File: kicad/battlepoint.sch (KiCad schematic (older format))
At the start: 26 parts, among them J1 BTNS, J2 TMR_LEDS, J3 CAP_LEDS, P13 BTNS_IN, P14 OLED_OUT, P17 BTNS_OUT, P20 AUX_PWR, P30 EXT_PWR_JP, P5 SPK, P8 AUDIO_JACK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

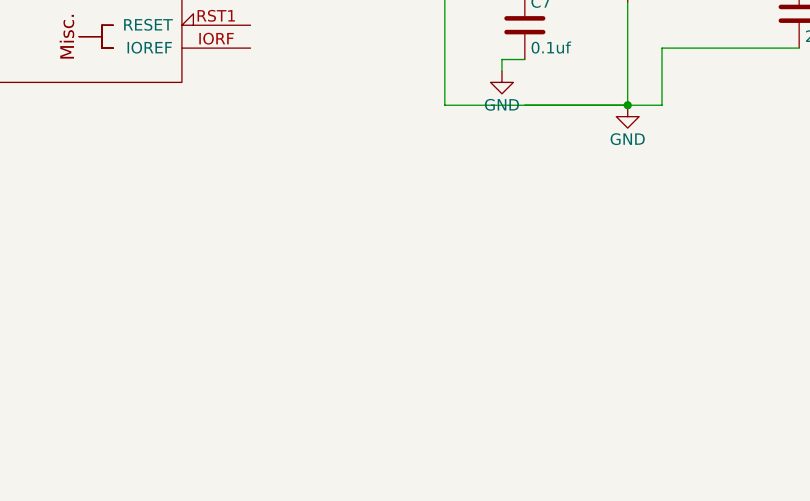
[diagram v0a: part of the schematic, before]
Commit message: reversed the top layer
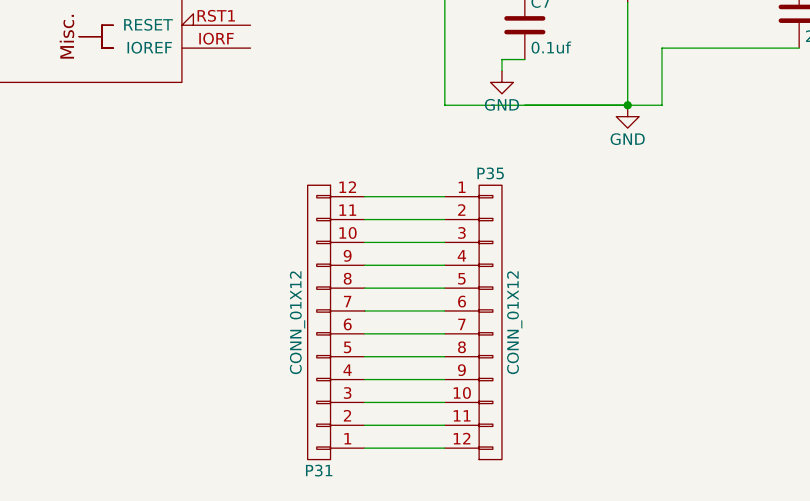
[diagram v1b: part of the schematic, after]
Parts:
- added P31, P35: CONN_01X12, Pin_Headers:Pin_Header_Straight_1x12, symbol CONN_01X12
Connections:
- new net: P31.1 (P1), P35.12 (P12)
- new net: P31.10 (P10), P35.3 (P3)
- new net: P31.11 (P11), P35.2 (P2)
- new net: P31.12 (P12), P35.1 (P1)
- new net: P31.2 (P2), P35.11 (P11)
- new net: P31.3 (P3), P35.10 (P10)
- new net: P31.4 (P4), P35.9 (P9)
- new net: P31.5 (P5), P35.8 (P8)
- new net: P31.6 (P6), P35.7 (P7)
- new net: P31.7 (P7), P35.6 (P6)
- new net: P31.8 (P8), P35.5 (P5)
- new net: P31.9 (P9), P35.4 (P4)

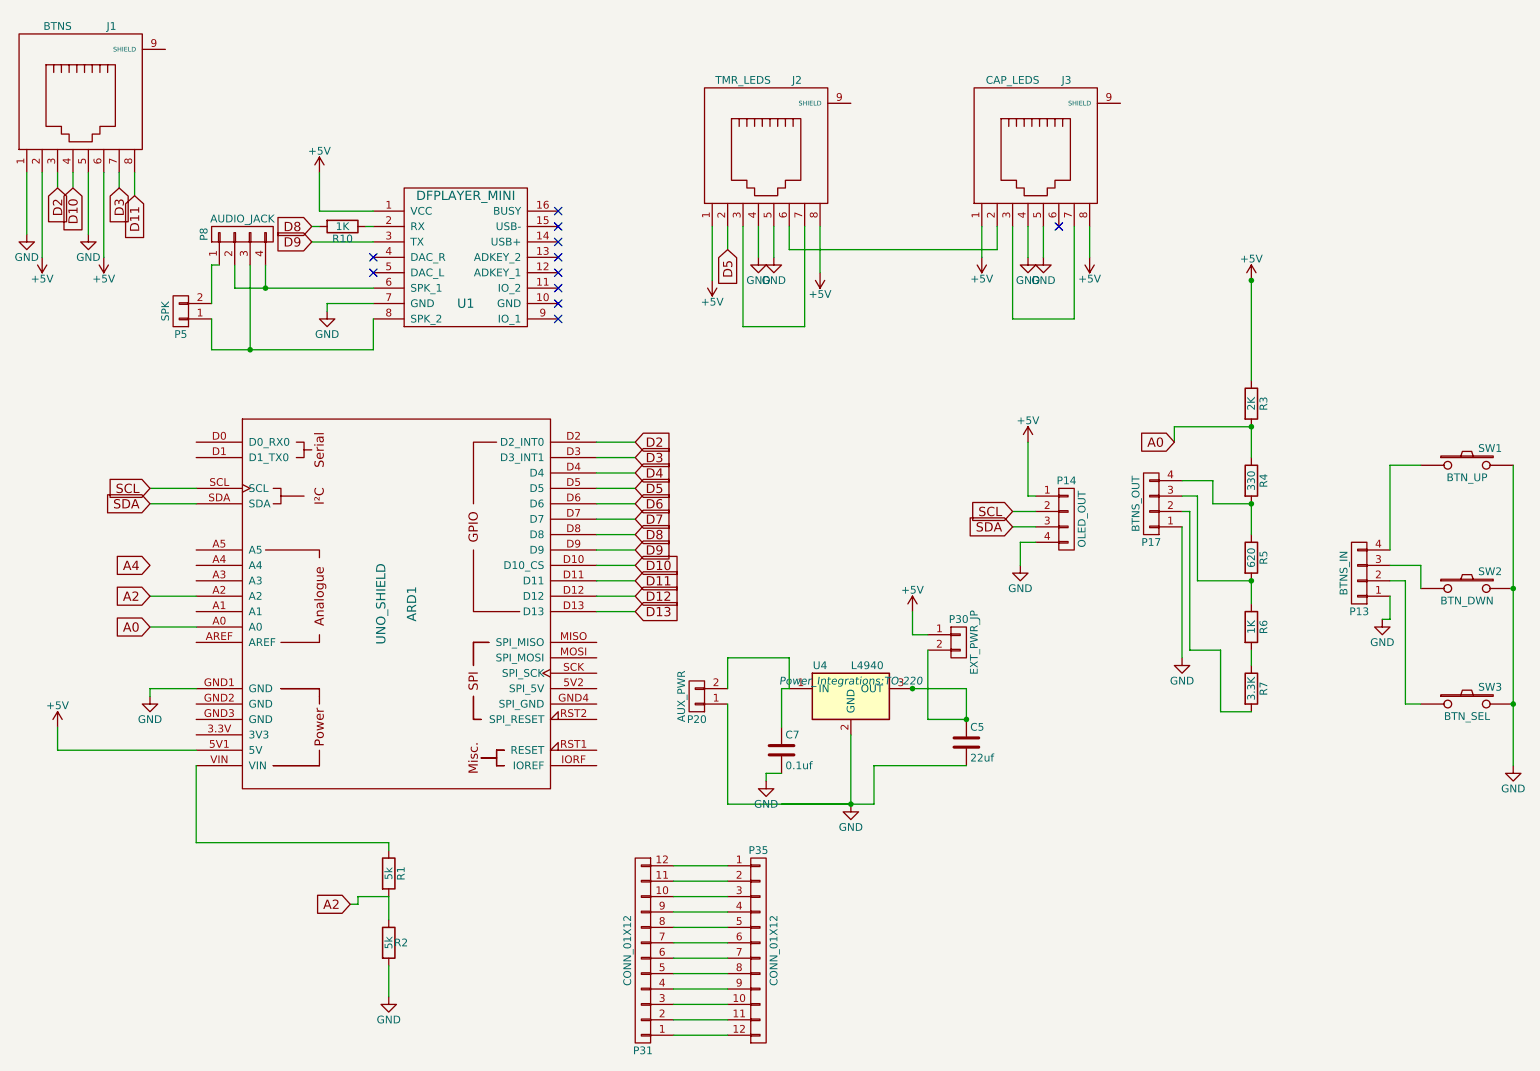
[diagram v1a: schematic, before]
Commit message: changed to usb connectors
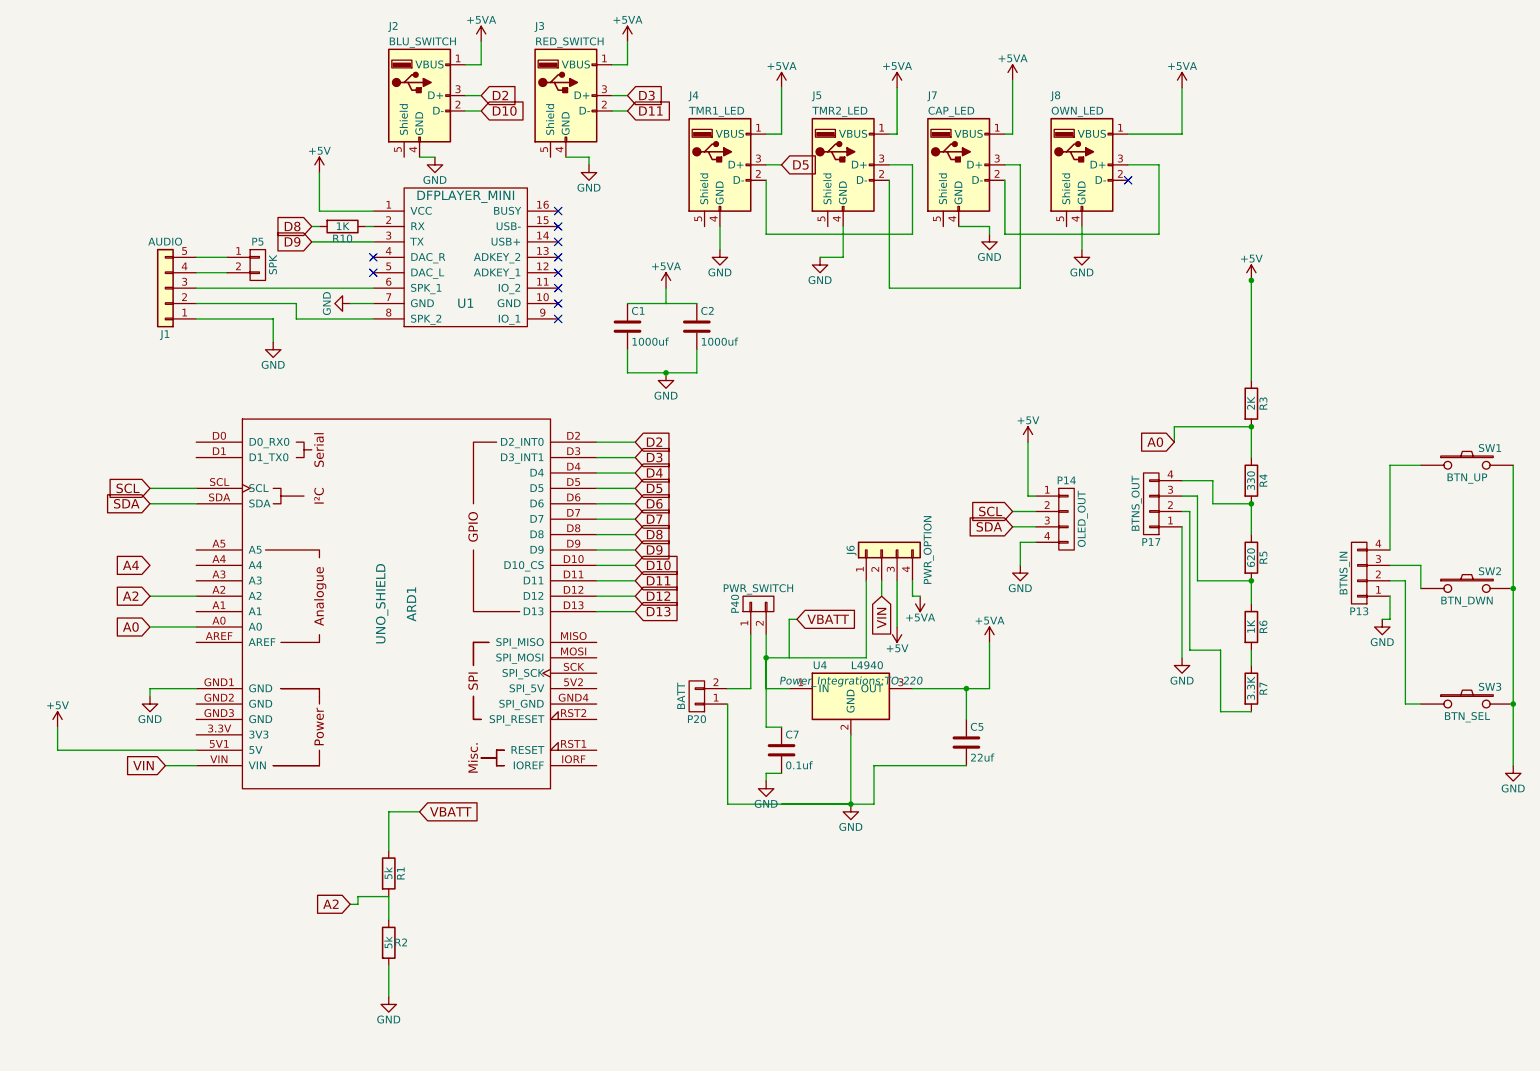
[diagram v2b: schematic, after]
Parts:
- removed J1: BTNS, Connect:RJ45_8, symbol RJ45
- removed J2: TMR_LEDS, Connect:RJ45_8, symbol RJ45
- removed J3: CAP_LEDS, Connect:RJ45_8, symbol RJ45
- removed P30: EXT_PWR_JP, Pin_Headers:Pin_Header_Straight_1x02, symbol CONN_01X02
- removed P31, P35: CONN_01X12, Pin_Headers:Pin_Header_Straight_1x12, symbol CONN_01X12
- removed P8: AUDIO_JACK, Connectors_JST:JST_XH_B04B-XH-A_04x2.50mm_Straight, symbol CONN_01X04
- added C1, C2: 1000uf, Capacitors_THT:CP_Radial_D7.5mm_P2.50mm, symbol C
- added J1: AUDIO, Connectors_JST:JST_XH_B05B-XH-A_05x2.50mm_Straight, symbol Conn_01x05
- added J2: BLU_SWITCH, Connectors:USB_A, symbol USB_A
- added J3: RED_SWITCH, Connectors:USB_A, symbol USB_A
- added J4: TMR1_LED, Connectors:USB_A, symbol USB_A
- added J5: TMR2_LED, Connectors:USB_A, symbol USB_A
- added J6: PWR_OPTION, Pin_Headers:Pin_Header_Straight_1x04_Pitch2.54mm, symbol Conn_01x04
- added J7: CAP_LED, Connectors:USB_A, symbol USB_A
- added J8: OWN_LED, Connectors:USB_A, symbol USB_A
- added P40: PWR_SWITCH, Connectors_JST:JST_XH_B02B-XH-A_02x2.50mm_Straight, symbol CONN_01X02
- P20: value AUX_PWR -> BATT
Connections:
- net +5V: now also J6.3 (Pin_3)
- net D10: now also J2.2 (D-)
- net D11: now also J3.2 (D-)
- net D2: now also J2.3 (D+)
- net D3: now also J3.3 (D+)
- net D5: now also J4.3 (D+)
- net GND: now also C1.2, C2.2, J1.1 (Pin_1), J2.4 (GND), J3.4 (GND), J4.4 (GND), J5.4 (GND), J7.4 (GND), J8.4 (GND)
- net VBATT: now reaches R1.1
- net VBATT: no longer ARD1.VIN
- net at U1.6 (SPK_1): now also J1.3 (Pin_3)
- net at U1.8 (SPK_2): now also J1.2 (Pin_2); no longer P5.1 (P1)
- net at P5.2 (P2): now also J1.4 (Pin_4)
- net at C7.1, U4.1 (IN): now also J6.1 (Pin_1), P40.2 (P2); no longer P20.2 (P2)
- net +5VA: now reaches C5.1, U4.3 (OUT)
- net +5VA: now also J2.1 (VBUS), J3.1 (VBUS), J4.1 (VBUS), J5.1 (VBUS), J6.4 (Pin_4), J7.1 (VBUS), J8.1 (VBUS)
- new net: J1.5 (Pin_5), P5.1 (P1)
- new net: P20.2 (P2), P40.1 (P1)
- new net: J4.2 (D-), J5.3 (D+)
- new net: J5.2 (D-), J7.3 (D+)
- new net: J7.2 (D-), J8.3 (D+)
- new net: C1.1, C2.1
- new net VIN: ARD1.VIN, J6.2 (Pin_2)
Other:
- moved on the sheet: P5
